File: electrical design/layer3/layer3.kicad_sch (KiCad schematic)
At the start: 42 parts, among them J12 XH2.54 2P, J13 LAYER1, J14 SH1.0 2P, J16 CAMERA1, J16 CAMERA2, J2 SH1.0 5P, J8 COMPASS, J9 XH2.54 2P, SW1 SW_SPDT, SW2 SW_DIP_x04, U1 TEENSY 4.0, U2 TEENSY 4.0, U3 MOUDLE-SEEEDUINO-XIAO-ESP32C3, U4 74LVC2G04, U4 MOUDLE-SEEEDUINO-XIAO-ESP32C3, U5 74LVC2G04, U6 74LVC2G04

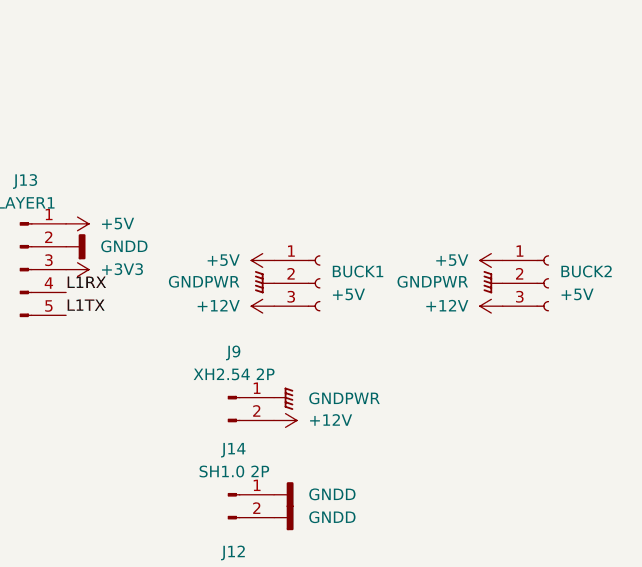
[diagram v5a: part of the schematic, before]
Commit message: amend buck conv pinouts on l1 and l3
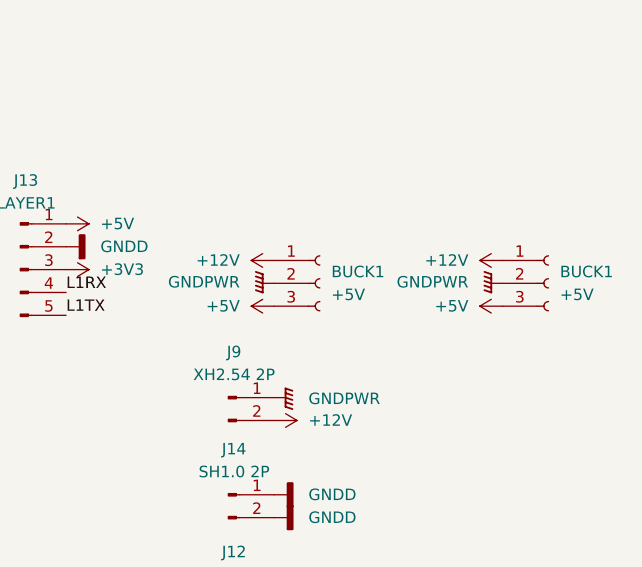
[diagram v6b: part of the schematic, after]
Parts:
- removed BUCK2: +5V, Connector_PinSocket_2.54mm:PinSocket_1x03_P2.54mm_Vertical, symbol Connector:Conn_01x03_Female
- added BUCK1: +5V, Connector_PinSocket_2.54mm:TPS5430 Board, symbol Connector:Conn_01x03_Female
- BUCK1: footprint Connector_PinSocket_2.54mm:PinSocket_1x03_P2.54mm_Vertical -> Connector_PinSocket_2.54mm:TPS5430 Board
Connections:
- net +12V: now also BUCK1.1 (Pin_1), BUCK1.1 (Pin_1); no longer BUCK1.3 (Pin_3)
- net +5V: now also BUCK1.3 (Pin_3), BUCK1.3 (Pin_3); no longer BUCK1.1 (Pin_1)
- net GNDPWR: now also BUCK1.2 (Pin_2)
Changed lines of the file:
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@@
     )
   )
-  (symbol (lib_name "+12V_2") (lib_id "power:+12V") (at 243.84 72.39 90) (unit 1)
-    (in_bom yes) (on_board yes) (dnp no) (fields_autoplaced)
-    (property "Reference" "#PWR023" (at 247.65 72.39 0)
-      (effects (font (size 1.27 1.27)) hide)
-    )
-    (property "Value" "+12V" (at 240.03 72.39 90)
-      (effects (font (size 1.27 1.27)) (justify left))
-    )
-    (property "Footprint" "" (at 243.84 72.39 0)
-      (effects (font (size 1.27 1.27)) hide)
-    )
-    (property "Datasheet" "" (at 243.84 72.39 0)
+  (symbol (lib_name "+12V_2") (lib_id "power:+12V") (at 243.84 67.31 90) (unit 1)
+    (in_bom yes) (on_board yes) (dnp no) (fields_autoplaced)
+    (property "Reference" "#PWR023" (at 247.65 67.31 0)
+      (effects (font (size 1.27 1.27)) hide)
+    )
+    (property "Value" "+12V" (at 240.03 67.31 90)
+      (effects (font (size 1.27 1.27)) (justify left))
+    )
+    (property "Footprint" "" (at 243.84 67.31 0)
+      (effects (font (size 1.27 1.27)) hide)
+    )
+    (property "Datasheet" "" (at 243.84 67.31 0)
       (effects (font (size 1.27 1.27)) hide)
     )
@@
     )
   )
+  (symbol (lib_name "+5V_1") (lib_id "power:+5V") (at 269.24 72.39 90) (unit 1)
+    (in_bom yes) (on_board yes) (dnp no) (fields_autoplaced)
+    (property "Reference" "#PWR08" (at 273.05 72.39 0)
+      (effects (font (size 1.27 1.27)) hide)
+    )
+    (property "Value" "+5V" (at 265.43 72.39 90)
+      (effects (font (size 1.27 1.27)) (justify left))
+    )
+    (property "Footprint" "" (at 269.24 72.39 0)
+      (effects (font (size 1.27 1.27)) hide)
+    )
+    (property "Datasheet" "" (at 269.24 72.39 0)
+      (effects (font (size 1.27 1.27)) hide)
+    )
+    (pin "1")
+    (instances
+      (project "layer3"
+        (path "/e63e39d7-6ac0-4ffd-8aa3-1841a4541b55"
+          (reference "#PWR08") (unit 1)
+        )
+      )
+    )
+  )
   (symbol (lib_id "MOUDLE-SEEEDUINO-XIAO-ESP32C3:MOUDLE-SEEEDUINO-XIAO-ESP32C3") (at 111.125 97.79 0) (unit 1)
     (in_bom yes) (on_board yes) (dnp no) (fields_autoplaced)
@@
     )
   )
-  (symbol (lib_name "+12V_2") (lib_id "power:+12V") (at 269.24 72.39 90) (unit 1)
-    (in_bom yes) (on_board yes) (dnp no) (fields_autoplaced)
-    (property "Reference" "#PWR024" (at 273.05 72.39 0)
-      (effects (font (size 1.27 1.27)) hide)
-    )
-    (property "Value" "+12V" (at 265.43 72.39 90)
-      (effects (font (size 1.27 1.27)) (justify left))
-    )
-    (property "Footprint" "" (at 269.24 72.39 0)
-      (effects (font (size 1.27 1.27)) hide)
-    )
-    (property "Datasheet" "" (at 269.24 72.39 0)
+  (symbol (lib_name "+12V_2") (lib_id "power:+12V") (at 269.24 67.31 90) (unit 1)
+    (in_bom yes) (on_board yes) (dnp no) (fields_autoplaced)
+    (property "Reference" "#PWR024" (at 273.05 67.31 0)
+      (effects (font (size 1.27 1.27)) hide)
+    )
+    (property "Value" "+12V" (at 265.43 67.31 90)
+      (effects (font (size 1.27 1.27)) (justify left))
+    )
+    (property "Footprint" "" (at 269.24 67.31 0)
+      (effects (font (size 1.27 1.27)) hide)
+    )
+    (property "Datasheet" "" (at 269.24 67.31 0)
       (effects (font (size 1.27 1.27)) hide)
     )
@@
         (path "/e63e39d7-6ac0-4ffd-8aa3-1841a4541b55"
           (reference "J6") (unit 1)
-        )
-      )
-    )
-  )
-  (symbol (lib_name "+5V_1") (lib_id "power:+5V") (at 269.24 67.31 90) (unit 1)
-    (in_bom yes) (on_board yes) (dnp no) (fields_autoplaced)
-    (property "Reference" "#PWR08" (at 273.05 67.31 0)
-      (effects (font (size 1.27 1.27)) hide)
-    )
-    (property "Value" "+5V" (at 265.43 67.31 90)
-      (effects (font (size 1.27 1.27)) (justify left))
-    )
-    (property "Footprint" "" (at 269.24 67.31 0)
-      (effects (font (size 1.27 1.27)) hide)
-    )
-    (property "Datasheet" "" (at 269.24 67.31 0)
-      (effects (font (size 1.27 1.27)) hide)
-    )
-    (pin "1")
-    (instances
-      (project "layer3"
-        (path "/e63e39d7-6ac0-4ffd-8aa3-1841a4541b55"
-          (reference "#PWR08") (unit 1)
         )
       )
@@
     )
   )
-  (symbol (lib_name "+5V_1") (lib_id "power:+5V") (at 243.84 67.31 90) (unit 1)
-    (in_bom yes) (on_board yes) (dnp no) (fields_autoplaced)
-    (property "Reference" "#PWR035" (at 247.65 67.31 0)
-      (effects (font (size 1.27 1.27)) hide)
-    )
-    (property "Value" "+5V" (at 240.03 67.31 90)
-      (effects (font (size 1.27 1.27)) (justify left))
-    )
-    (property "Footprint" "" (at 243.84 67.31 0)
-      (effects (font (size 1.27 1.27)) hide)
-    )
-    (property "Datasheet" "" (at 243.84 67.31 0)
+  (symbol (lib_name "+5V_1") (lib_id "power:+5V") (at 243.84 72.39 90) (unit 1)
+    (in_bom yes) (on_board yes) (dnp no) (fields_autoplaced)
+    (property "Reference" "#PWR035" (at 247.65 72.39 0)
+      (effects (font (size 1.27 1.27)) hide)
+    )
+    (property "Value" "+5V" (at 240.03 72.39 90)
+      (effects (font (size 1.27 1.27)) (justify left))
+    )
+    (property "Footprint" "" (at 243.84 72.39 0)
+      (effects (font (size 1.27 1.27)) hide)
+    )
+    (property "Datasheet" "" (at 243.84 72.39 0)
       (effects (font (size 1.27 1.27)) hide)
     )
@@
       (effects (font (size 1.27 1.27)) (justify left))
     )
-    (property "Footprint" "Connector_PinSocket_2.54mm:PinSocket_1x03_P2.54mm_Vertical" (at 248.92 69.85 0)
+    (property "Footprint" "Connector_PinSocket_2.54mm:TPS5430 Board" (at 248.92 69.85 0)
       (effects (font (size 1.27 1.27)) hide)
     )
@@
     )
   )
+  (symbol (lib_id "Connector:Conn_01x03_Female") (at 274.32 69.85 0) (unit 1)
+    (in_bom yes) (on_board yes) (dnp no) (fields_autoplaced)
+    (property "Reference" "BUCK1" (at 275.59 68.58 0)
+      (effects (font (size 1.27 1.27)) (justify left))
+    )
+    (property "Value" "+5V" (at 275.59 71.12 0)
+      (effects (font (size 1.27 1.27)) (justify left))
+    )
+    (property "Footprint" "Connector_PinSocket_2.54mm:TPS5430 Board" (at 274.32 69.85 0)
+      (effects (font (size 1.27 1.27)) hide)
+    )
+    (property "Datasheet" "~" (at 274.32 69.85 0)
+      (effects (font (size 1.27 1.27)) hide)
+    )
+    (pin "1")
+    (pin "2")
+    (pin "3")
+    (instances
+      (project "layer1"
+        (path "/32d54464-fd6f-441d-9cef-d3e4fabf9fe1"
+          (reference "BUCK1") (unit 1)
+        )
+      )
+      (project "layer3"
+        (path "/d3bc7e0f-ae6c-4cdf-9591-eb9484f67211"
+          (reference "BUCK1") (unit 1)
+        )
+      )
+      (project "layer3"
+        (path "/e63e39d7-6ac0-4ffd-8aa3-1841a4541b55"
+          (reference "BUCK2") (unit 1)
+        )
+      )
+    )
+  )
   (symbol (lib_id "power:GNDD") (at 80.01 67.31 90) (unit 1)
     (in_bom yes) (on_board yes) (dnp no) (fields_autoplaced)
@@
         )
       )
-    )
-  )
-  (symbol (lib_id "Connector:Conn_01x03_Female") (at 274.32 69.85 0) (unit 1)
-    (in_bom yes) (on_board yes) (dnp no) (fields_autoplaced)
-    (property "Reference" "BUCK2" (at 275.59 68.58 0)
-      (effects (font (size 1.27 1.27)) (justify left))
-    )
-    (property "Value" "+5V" (at 275.59 71.12 0)
-      (effects (font (size 1.27 1.27)) (justify left))
-    )
-    (property "Footprint" "Connector_PinSocket_2.54mm:PinSocket_1x03_P2.54mm_Vertical" (at 274.32 69.85 0)
-      (effects (font (size 1.27 1.27)) hide)
-    )
-    (property "Datasheet" "~" (at 274.32 69.85 0)
-      (effects (font (size 1.27 1.27)) hide)
-    )
-    (pin "1")
-    (pin "2")
-    (pin "3")
-    (instances
-      (project "layer1"
-        (path "/32d54464-fd6f-441d-9cef-d3e4fabf9fe1"
-          (reference "BUCK2") (unit 1)
-        )
-      )
-      (project "layer3"
-        (path "/d3bc7e0f-ae6c-4cdf-9591-eb9484f67211"
-          (reference "BUCK2") (unit 1)
-        )
-      )
-      (project "layer3"
-        (path "/e63e39d7-6ac0-4ffd-8aa3-1841a4541b55"
-          (reference "BUCK2") (unit 1)
-        )
-      )

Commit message: reroute 90 deg traces on l3 pcb
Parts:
- J12: footprint Connector_Wire:SolderWire-0.5sqmm_1x02_P4.6mm_D0.9mm_OD2.1mm -> Connector_JST:JST_XH_B2B-XH-A_1x02_P2.50mm_Vertical
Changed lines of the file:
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@@
       (effects (font (size 1.27 1.27)))
     )
-    (property "Footprint" "Connector_Wire:SolderWire-0.5sqmm_1x02_P4.6mm_D0.9mm_OD2.1mm" (at 238.76 104.775 0)
+    (property "Footprint" "Connector_JST:JST_XH_B2B-XH-A_1x02_P2.50mm_Vertical" (at 238.76 104.775 0)
       (effects (font (size 1.27 1.27)) hide)
     )

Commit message: finalise pcbs for production
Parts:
- J13: value LAYER1 -> SH1.0 5P
- U1, U2: footprint teensy:Teensy40 -> MODULE_DEV-15583
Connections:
- net +3V3: no longer U1.3.3V_1, U2.3.3V_1
- net GNDD: no longer U1.G2, U2.G2
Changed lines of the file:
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@@
       (effects (font (size 1.27 1.27)))
     )
-    (property "Footprint" "teensy:Teensy40" (at 46.99 158.75 0)
+    (property "Footprint" "MODULE_DEV-15583" (at 46.99 158.75 0)
       (effects (font (size 1.27 1.27)) (justify bottom) hide)
     )
@@
     (pin "VIN")
     (pin "10")
-    (pin "PGM")
     (pin "G1")
     (pin "7")
@@
     (pin "6")
     (pin "5")
-    (pin "VBAT")
     (pin "4")
     (pin "1")
-    (pin "ON-OFF")
     (pin "3")
-    (pin "3.3V_1")
     (pin "14")
     (pin "18")
@@
     (pin "21")
     (pin "23")
-    (pin "G2")
     (pin "8")
     (pin "G3")
@@
         (path "/e63e39d7-6ac0-4ffd-8aa3-1841a4541b55"
           (reference "J8") (unit 1)
-        )
-      )
-    )
-  )
-  (symbol (lib_id "power:+3V3") (at 29.21 123.19 90) (unit 1)
-    (in_bom yes) (on_board yes) (dnp no) (fields_autoplaced)
-    (property "Reference" "#PWR0101" (at 33.02 123.19 0)
-      (effects (font (size 1.27 1.27)) hide)
-    )
-    (property "Value" "+3V3" (at 25.4 123.1899 90)
-      (effects (font (size 1.27 1.27)) (justify left))
-    )
-    (property "Footprint" "" (at 29.21 123.19 0)
-      (effects (font (size 1.27 1.27)) hide)
-    )
-    (property "Datasheet" "" (at 29.21 123.19 0)
-      (effects (font (size 1.27 1.27)) hide)
-    )
-    (pin "1")
-    (instances
-      (project "layer3"
-        (path "/d3bc7e0f-ae6c-4cdf-9591-eb9484f67211"
-          (reference "#PWR0101") (unit 1)
-        )
-      )
-      (project "layer3"
-        (path "/e63e39d7-6ac0-4ffd-8aa3-1841a4541b55"
-          (reference "#PWR012") (unit 1)
         )
       )
@@
     )
   )
-  (symbol (lib_id "power:+3V3") (at 29.21 179.07 90) (unit 1)
-    (in_bom yes) (on_board yes) (dnp no) (fields_autoplaced)
-    (property "Reference" "#PWR0101" (at 33.02 179.07 0)
-      (effects (font (size 1.27 1.27)) hide)
-    )
-    (property "Value" "+3V3" (at 25.4 179.0699 90)
-      (effects (font (size 1.27 1.27)) (justify left))
-    )
-    (property "Footprint" "" (at 29.21 179.07 0)
-      (effects (font (size 1.27 1.27)) hide)
-    )
-    (property "Datasheet" "" (at 29.21 179.07 0)
-      (effects (font (size 1.27 1.27)) hide)
-    )
-    (pin "1")
-    (instances
-      (project "layer3"
-        (path "/d3bc7e0f-ae6c-4cdf-9591-eb9484f67211"
-          (reference "#PWR0101") (unit 1)
-        )
-      )
-      (project "layer3"
-        (path "/e63e39d7-6ac0-4ffd-8aa3-1841a4541b55"
-          (reference "#PWR042") (unit 1)
-        )
-      )
-    )
-  )
   (symbol (lib_id "power:GNDD") (at 140.335 123.825 270) (unit 1)
     (in_bom yes) (on_board yes) (dnp no) (fields_autoplaced)
@@
       (effects (font (size 1.27 1.27)))
     )
-    (property "Footprint" "teensy:Teensy40" (at 46.99 102.87 0)
+    (property "Footprint" "MODULE_DEV-15583" (at 46.99 102.87 0)
       (effects (font (size 1.27 1.27)) (justify left bottom) hide)
     )
@@
     (pin "23")
     (pin "3")
-    (pin "3.3V_1")
     (pin "3.3V_2")
     (pin "4")
@@
     (pin "9")
     (pin "G1")
-    (pin "G2")
     (pin "G3")
-    (pin "ON-OFF")
-    (pin "PGM")
-    (pin "VBAT")
     (pin "VIN")
     (instances
@@
     )
   )
-  (symbol (lib_id "power:GNDD") (at 29.21 181.61 270) (unit 1)
-    (in_bom yes) (on_board yes) (dnp no) (fields_autoplaced)
-    (property "Reference" "#PWR043" (at 22.86 181.61 0)
-      (effects (font (size 1.27 1.27)) hide)
-    )
-    (property "Value" "GNDD" (at 25.4 181.61 90)
-      (effects (font (size 1.27 1.27)) (justify right))
-    )
-    (property "Footprint" "" (at 29.21 181.61 0)
-      (effects (font (size 1.27 1.27)) hide)
-    )
-    (property "Datasheet" "" (at 29.21 181.61 0)
-      (effects (font (size 1.27 1.27)) hide)
-    )
-    (pin "1")
-    (instances
-      (project "layer3"
-        (path "/e63e39d7-6ac0-4ffd-8aa3-1841a4541b55"
-          (reference "#PWR043") (unit 1)
-        )
-      )
-    )
-  )
   (symbol (lib_id "power:+3V3") (at 64.77 87.63 270) (unit 1)
     (in_bom yes) (on_board yes) (dnp no) (fields_autoplaced)
@@
       (effects (font (size 1.27 1.27)))
     )
-    (property "Value" "LAYER1" (at 216.281 60.96 0)
+    (property "Value" "SH1.0 5P" (at 216.281 60.96 0)
       (effects (font (size 1.27 1.27)))
     )
@@
         )
       )
-    )
-  )
-  (symbol (lib_id "power:GNDD") (at 29.21 125.73 270) (unit 1)
-    (in_bom yes) (on_board yes) (dnp no) (fields_autoplaced)
-    (property "Reference" "#PWR013" (at 22.86 125.73 0)
-      (effects (font (size 1.27 1.27)) hide)
-    )
-    (property "Value" "GNDD" (at 25.4 125.73 90)
-      (effects (font (size 1.27 1.27)) (justify right))
-    )
-    (property "Footprint" "" (at 29.21 125.73 0)
-      (effects (font (size 1.27 1.27)) hide)
-    )
-    (property "Datasheet" "" (at 29.21 125.73 0)
-      (effects (font (size 1.27 1.27)) hide)
-    )
-    (pin "1")
-    (instances
-      (project "layer3"
-        (path "/e63e39d7-6ac0-4ffd-8aa3-1841a4541b55"
-          (reference "#PWR013") (unit 1)
-        )
-      )
